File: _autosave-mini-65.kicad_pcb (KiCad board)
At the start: 2 copper layers, 308 x 98.4 mm, 170 parts, among them J1 TYPE-C-31-M12_13_EDITED, J2 AVR-ISP-6, SW1 SW_Push, U1 ATmega32U4-AU, U2 USBLC6-2SC6, Y1 Crystal_GND24_Small

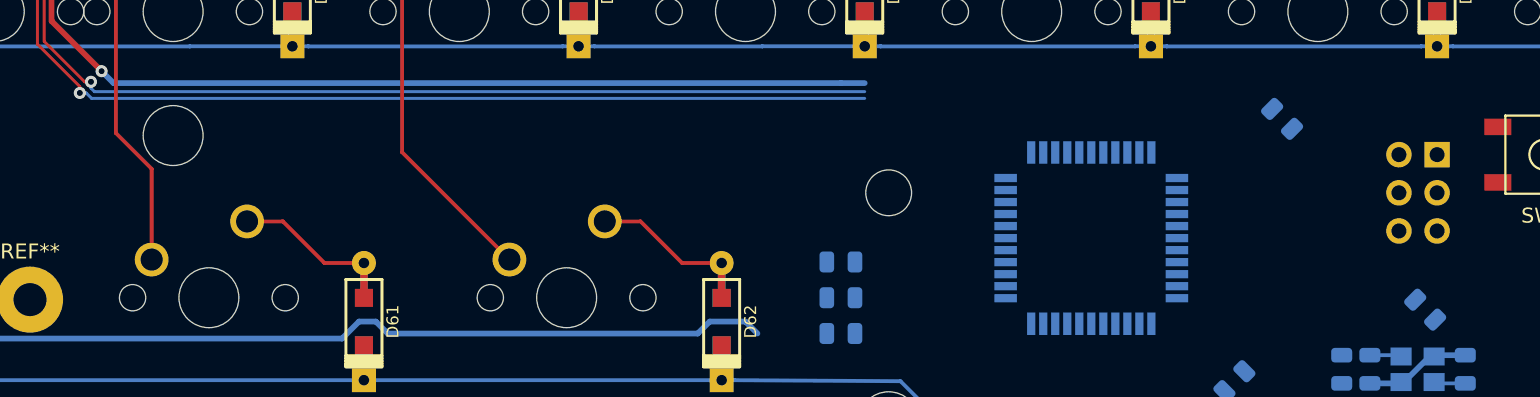
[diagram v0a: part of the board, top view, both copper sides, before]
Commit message: USB data lies routed
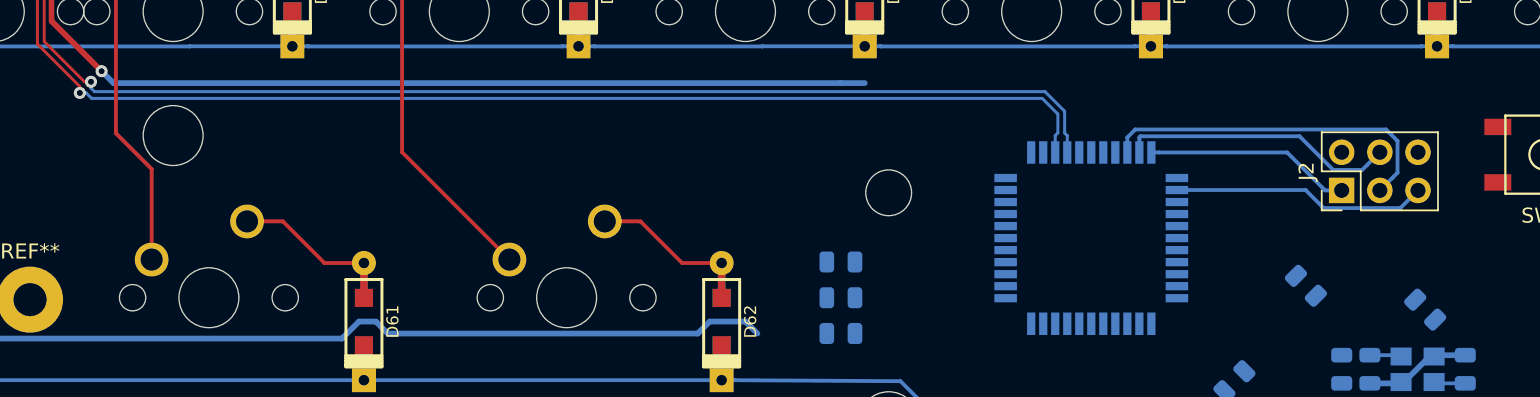
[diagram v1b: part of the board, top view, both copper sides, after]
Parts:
- J2: moved to F.Cu
- moved C5 11.2 mm to (29.4, 164.3)
- moved J2 6.78 mm to (31.8, 158.0), turned to 90 degrees
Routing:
- net SCK: track 0.00 -> 23.3 mm
- net MOSI: track 0.00 -> 18.5 mm
- net RESET: track 0.00 -> 17.0 mm
- net DP: track 123.8 -> 140.5 mm
- net DN: track 124.6 -> 140.5 mm
- net MISO: track 0.00 -> 13.7 mm
